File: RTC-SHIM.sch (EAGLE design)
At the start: 17 parts, among them IC1 DS3231/SO, IC2 DS3231M

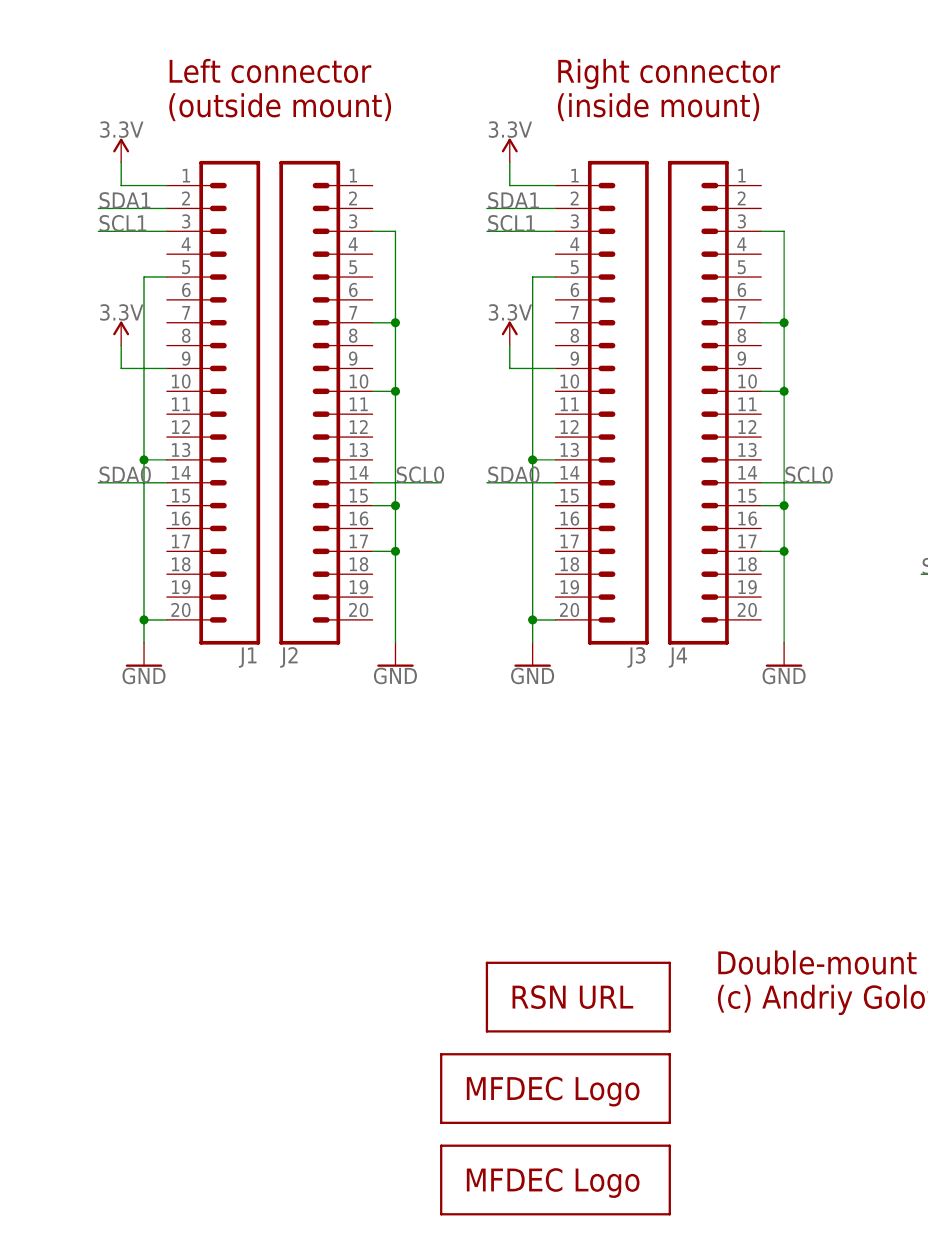
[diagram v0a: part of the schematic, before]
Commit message: Use more locking pin headers. Moved some traces.
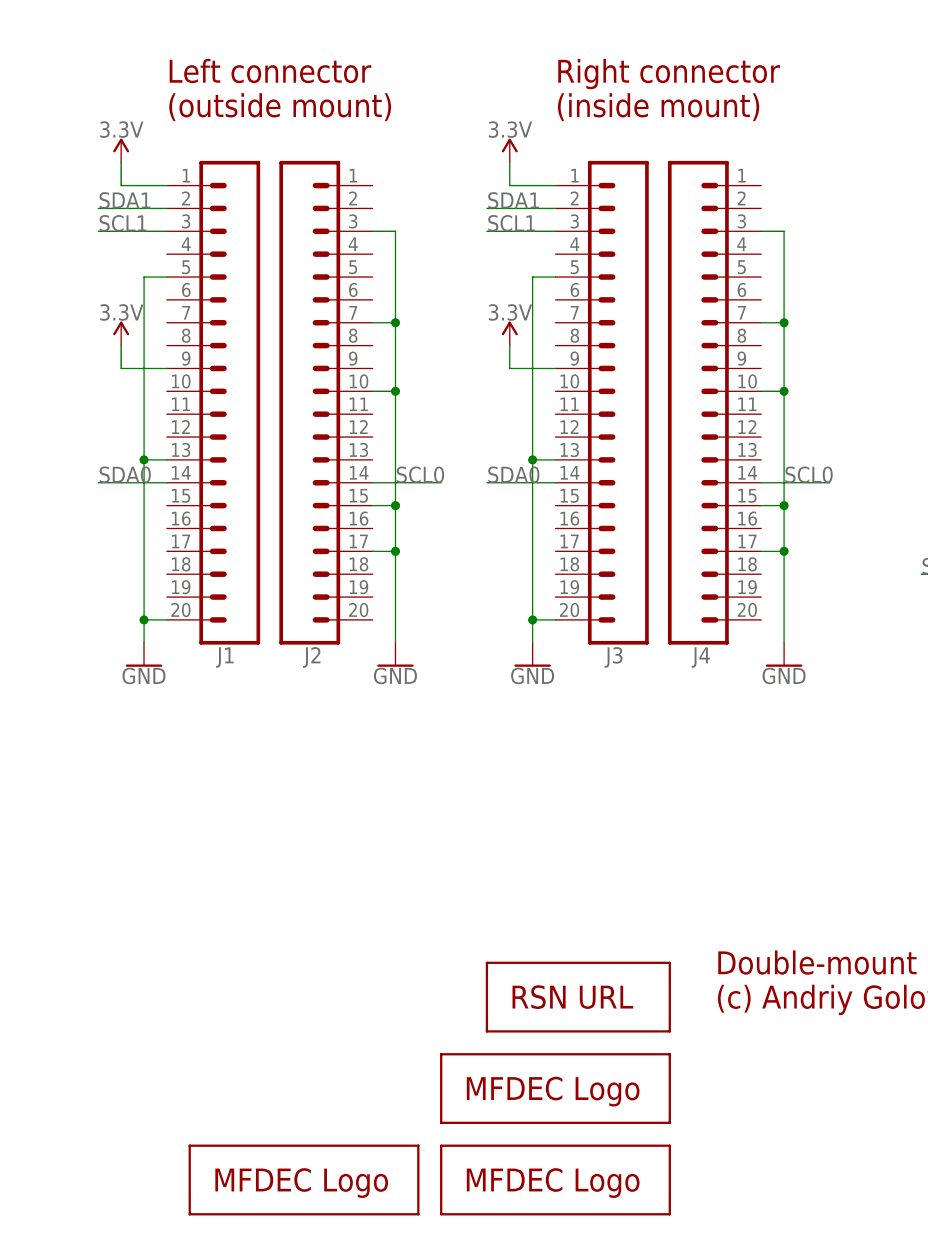
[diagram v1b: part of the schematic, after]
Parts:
- added LOGO4: MFDECLOGO_L_10MM, _my_logos:MFDECLOGO_L_10MM
- J1, J2, J3, J4: device SparkFun-Connectors:CONN_20LOCK_NOSILK -> _my_locked_connectors:CONN_20LOCK
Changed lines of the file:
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@@
 <layer number="115" name="ReferenceISLANDS" color="7" fill="1" visible="no" active="yes"/>
 <layer number="116" name="Patch_BOT" color="9" fill="4" visible="no" active="yes"/>
+<layer number="117" name="PM_Ref" color="7" fill="1" visible="no" active="no"/>
 <layer number="118" name="Rect_Pads" color="7" fill="1" visible="no" active="no"/>
+<layer number="119" name="PF_Ref" color="7" fill="1" visible="no" active="no"/>
+<layer number="120" name="WFL_Ref" color="7" fill="1" visible="no" active="no"/>
 <layer number="121" name="_tsilk" color="7" fill="1" visible="no" active="yes"/>
 <layer number="122" name="_bsilk" color="7" fill="1" visible="no" active="yes"/>
@@
 <layer number="128" name="_bValues" color="7" fill="1" visible="no" active="yes"/>
 <layer number="129" name="Mask" color="7" fill="1" visible="yes" active="yes"/>
+<layer number="130" name="SMDSTROOK" color="7" fill="1" visible="no" active="no"/>
 <layer number="131" name="tAdjust" color="7" fill="1" visible="no" active="yes"/>
 <layer number="132" name="bAdjust" color="7" fill="1" visible="no" active="yes"/>
+<layer number="133" name="bottom_silk" color="7" fill="1" visible="no" active="no"/>
+<layer number="134" name="silk_top" color="7" fill="1" visible="no" active="no"/>
+<layer number="135" name="silk_bottom" color="7" fill="1" visible="no" active="no"/>
+<layer number="136" name="silktop" color="7" fill="1" visible="no" active="no"/>
+<layer number="137" name="silkbottom" color="7" fill="1" visible="no" active="no"/>
+<layer number="138" name="EEE" color="7" fill="1" visible="no" active="no"/>
+<layer number="139" name="_tKeepout" color="7" fill="1" visible="no" active="no"/>
+<layer number="140" name="mbKeepout" color="7" fill="1" visible="no" active="no"/>
+<layer number="141" name="ASSEMBLY_TOP" color="7" fill="1" visible="no" active="no"/>
+<layer number="142" name="mbRestrict" color="7" fill="1" visible="no" active="no"/>
+<layer number="143" name="PLACE_BOUND_TOP" color="7" fill="1" visible="no" active="no"/>
 <layer number="144" name="Drill_legend" color="7" fill="1" visible="no" active="yes"/>
+<layer number="145" name="DrillLegend_01-16" color="7" fill="1" visible="no" active="no"/>
+<layer number="146" name="DrillLegend_01-20" color="7" fill="1" visible="no" active="no"/>
+<layer number="147" name="PIN_NUMBER" color="7" fill="1" visible="no" active="no"/>
+<layer number="148" name="DrillLegend_01-20" color="7" fill="1" visible="no" active="no"/>
+<layer number="149" name="DrillLegend_02-15" color="7" fill="1" visible="no" active="no"/>
 <layer number="150" name="Notes" color="7" fill="1" visible="no" active="yes"/>
 <layer number="151" name="HeatSink" color="7" fill="1" visible="no" active="yes"/>
@@
 <layer number="164" name="tRubout" color="7" fill="1" visible="yes" active="yes"/>
 <layer number="165" name="bRubout" color="7" fill="1" visible="yes" active="yes"/>
+<layer number="166" name="AntennaArea" color="7" fill="1" visible="no" active="no"/>
 <layer number="167" name="Fiducials" color="7" fill="1" visible="yes" active="yes"/>
+<layer number="168" name="4mmHeightArea" color="7" fill="1" visible="no" active="no"/>
 <layer number="169" name="internal" color="7" fill="1" visible="yes" active="yes"/>
+<layer number="191" name="mNets" color="7" fill="1" visible="no" active="no"/>
+<layer number="192" name="mBusses" color="7" fill="1" visible="no" active="no"/>
+<layer number="193" name="mPins" color="7" fill="1" visible="no" active="no"/>
+<layer number="194" name="mSymbols" color="7" fill="1" visible="no" active="no"/>
+<layer number="195" name="mNames" color="7" fill="1" visible="no" active="no"/>
+<layer number="196" name="mValues" color="7" fill="1" visible="no" active="no"/>
 <layer number="199" name="Contour" color="7" fill="1" visible="no" active="yes"/>
 <layer number="200" name="200bmp" color="1" fill="10" visible="no" active="yes"/>
@@
 <part name="SUPPLY4" library="SparkFun-PowerSymbols" library_urn="urn:adsk.eagle:library:530" deviceset="3.3V" device=""/>
 <part name="SUPPLY5" library="SparkFun-PowerSymbols" library_urn="urn:adsk.eagle:library:530" deviceset="3.3V" device=""/>
-<part name="J1" library="SparkFun-Connectors" library_urn="urn:adsk.eagle:library:513" deviceset="CONN_20" device="LOCK_NOSILK" package3d_urn="urn:adsk.eagle:package:38201/1"/>
-<part name="J2" library="SparkFun-Connectors" library_urn="urn:adsk.eagle:library:513" deviceset="CONN_20" device="LOCK_NOSILK" package3d_urn="urn:adsk.eagle:package:38201/1"/>
+<part name="J1" library="_my_locked_connectors" deviceset="CONN_20" device="LOCK"/>
+<part name="J2" library="_my_locked_connectors" deviceset="CONN_20" device="LOCK"/>
 <part name="SUPPLY6" library="SparkFun-PowerSymbols" library_urn="urn:adsk.eagle:library:530" deviceset="3.3V" device=""/>
 <part name="SUPPLY7" library="SparkFun-PowerSymbols" library_urn="urn:adsk.eagle:library:530" deviceset="3.3V" device=""/>
 <part name="GND5" library="SparkFun-PowerSymbols" library_urn="urn:adsk.eagle:library:530" deviceset="GND" device=""/>
 <part name="GND6" library="SparkFun-PowerSymbols" library_urn="urn:adsk.eagle:library:530" deviceset="GND" device=""/>
-<part name="J3" library="SparkFun-Connectors" library_urn="urn:adsk.eagle:library:513" deviceset="CONN_20" device="LOCK_NOSILK" package3d_urn="urn:adsk.eagle:package:38201/1"/>
-<part name="J4" library="SparkFun-Connectors" library_urn="urn:adsk.eagle:library:513" deviceset="CONN_20" device="LOCK_NOSILK" package3d_urn="urn:adsk.eagle:package:38201/1"/>
+<part name="J3" library="_my_locked_connectors" deviceset="CONN_20" device="LOCK"/>
+<part name="J4" library="_my_locked_connectors" deviceset="CONN_20" device="LOCK"/>
 <part name="SUPPLY8" library="SparkFun-PowerSymbols" library_urn="urn:adsk.eagle:library:530" deviceset="3.3V" device=""/>
 <part name="SUPPLY9" library="SparkFun-PowerSymbols" library_urn="urn:adsk.eagle:library:530" deviceset="3.3V" device=""/>
@@
 <part name="SUPPLY10" library="SparkFun-PowerSymbols" library_urn="urn:adsk.eagle:library:530" deviceset="3.3V" device=""/>
 <part name="GND10" library="SparkFun-PowerSymbols" library_urn="urn:adsk.eagle:library:530" deviceset="GND" device=""/>
+<part name="LOGO4" library="_my_logos" deviceset="MFDECLOGO" device="_L_10MM"/>
 </parts>
 <sheets>
@@
 <attribute name="VALUE" x="66.04" y="51.054" size="1.778" layer="96" align="bottom-center"/>
 </instance>
-<instance part="J1" gate="G$1" x="114.3" y="121.92" smashed="yes" rot="R180">
-<attribute name="VALUE" x="114.3" y="121.666" size="1.778" layer="96" font="vector" rot="R180"/>
-<attribute name="NAME" x="114.3" y="65.532" size="1.778" layer="95" rot="R180"/>
-</instance>
-<instance part="J2" gate="G$1" x="116.84" y="121.92" smashed="yes" rot="MR180">
-<attribute name="VALUE" x="116.84" y="121.666" size="1.778" layer="96" font="vector" rot="MR180"/>
-<attribute name="NAME" x="116.84" y="65.532" size="1.778" layer="95" rot="MR180"/>
+<instance part="J1" gate="G$1" x="111.76" y="91.44" smashed="yes" rot="R180">
+<attribute name="VALUE" x="111.76" y="91.186" size="1.778" layer="96" font="vector" rot="R180"/>
+<attribute name="NAME" x="111.76" y="65.532" size="1.778" layer="95" rot="R180"/>
+</instance>
+<instance part="J2" gate="G$1" x="119.38" y="91.44" smashed="yes" rot="MR180">
+<attribute name="VALUE" x="119.38" y="91.186" size="1.778" layer="96" font="vector" rot="MR180"/>
+<attribute name="NAME" x="119.38" y="65.532" size="1.778" layer="95" rot="MR180"/>
 </instance>
 <instance part="SUPPLY6" gate="G$1" x="99.06" y="119.38" smashed="yes">
@@
 <attribute name="VALUE" x="129.54" y="63.246" size="1.778" layer="96" align="top-center"/>
 </instance>
-<instance part="J3" gate="G$1" x="157.48" y="121.92" smashed="yes" rot="R180">
-<attribute name="VALUE" x="157.48" y="121.666" size="1.778" layer="96" font="vector" rot="R180"/>
-<attribute name="NAME" x="157.48" y="65.532" size="1.778" layer="95" rot="R180"/>
-</instance>
-<instance part="J4" gate="G$1" x="160.02" y="121.92" smashed="yes" rot="MR180">
-<attribute name="VALUE" x="160.02" y="121.666" size="1.778" layer="96" font="vector" rot="MR180"/>
-<attribute name="NAME" x="160.02" y="65.532" size="1.778" layer="95" rot="MR180"/>
+<instance part="J3" gate="G$1" x="154.94" y="91.44" smashed="yes" rot="R180">
+<attribute name="VALUE" x="154.94" y="91.186" size="1.778" layer="96" font="vector" rot="R180"/>
+<attribute name="NAME" x="154.94" y="65.532" size="1.778" layer="95" rot="R180"/>
+</instance>
+<instance part="J4" gate="G$1" x="162.56" y="91.44" smashed="yes" rot="MR180">
+<attribute name="VALUE" x="162.56" y="91.186" size="1.778" layer="96" font="vector" rot="MR180"/>
+<attribute name="NAME" x="162.56" y="65.532" size="1.778" layer="95" rot="MR180"/>
 </instance>
 <instance part="SUPPLY8" gate="G$1" x="142.24" y="119.38" smashed="yes">
@@
 <attribute name="VALUE" x="66.04" y="73.406" size="1.778" layer="96" align="top-center"/>
 </instance>
+<instance part="LOGO4" gate="G$1" x="106.68" y="2.54" smashed="yes"/>
 </instances>
 <busses>

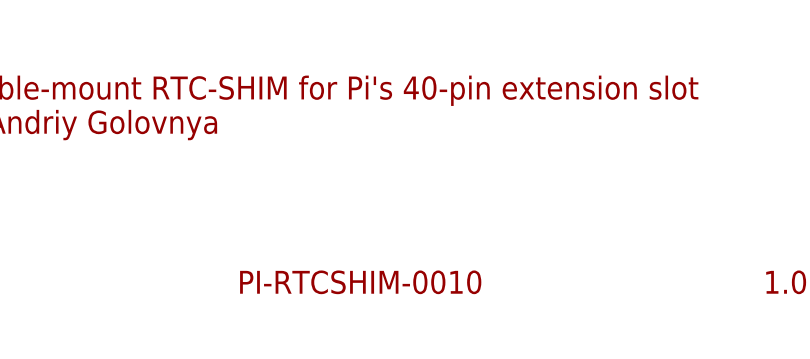
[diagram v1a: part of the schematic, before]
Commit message: Simplified document names. Generated PDF schematics.
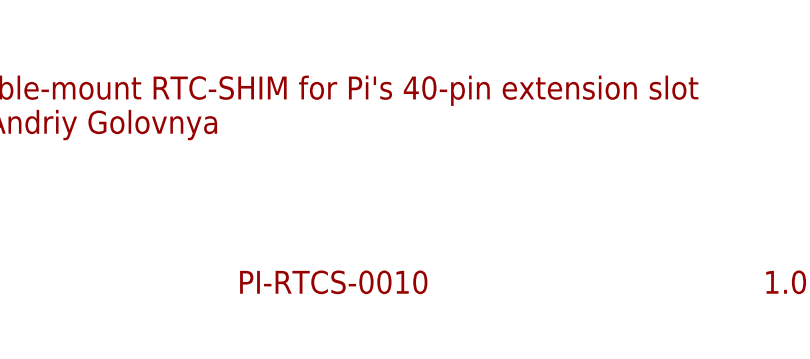
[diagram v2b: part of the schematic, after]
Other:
- note added: "PI-RTCS-0010"
- note removed: "PI-RTCSHIM-0010"
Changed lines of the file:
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@@
 <plain>
 <text x="256.54" y="7.62" size="2.54" layer="94">1.0</text>
-<text x="198.12" y="7.62" size="2.54" layer="94">PI-RTCSHIM-0010</text>
+<text x="198.12" y="7.62" size="2.54" layer="94">PI-RTCS-0010</text>
 <text x="165.1" y="25.4" size="2.54" layer="94">Double-mount RTC-SHIM for Pi's 40-pin extension slot
 (c) Andriy Golovnya</text>
